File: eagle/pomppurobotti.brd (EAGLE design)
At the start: 66.3 x 70.5 mm, 23 parts, among them Q1 MOSFET-NCHANNELFQP30N06L

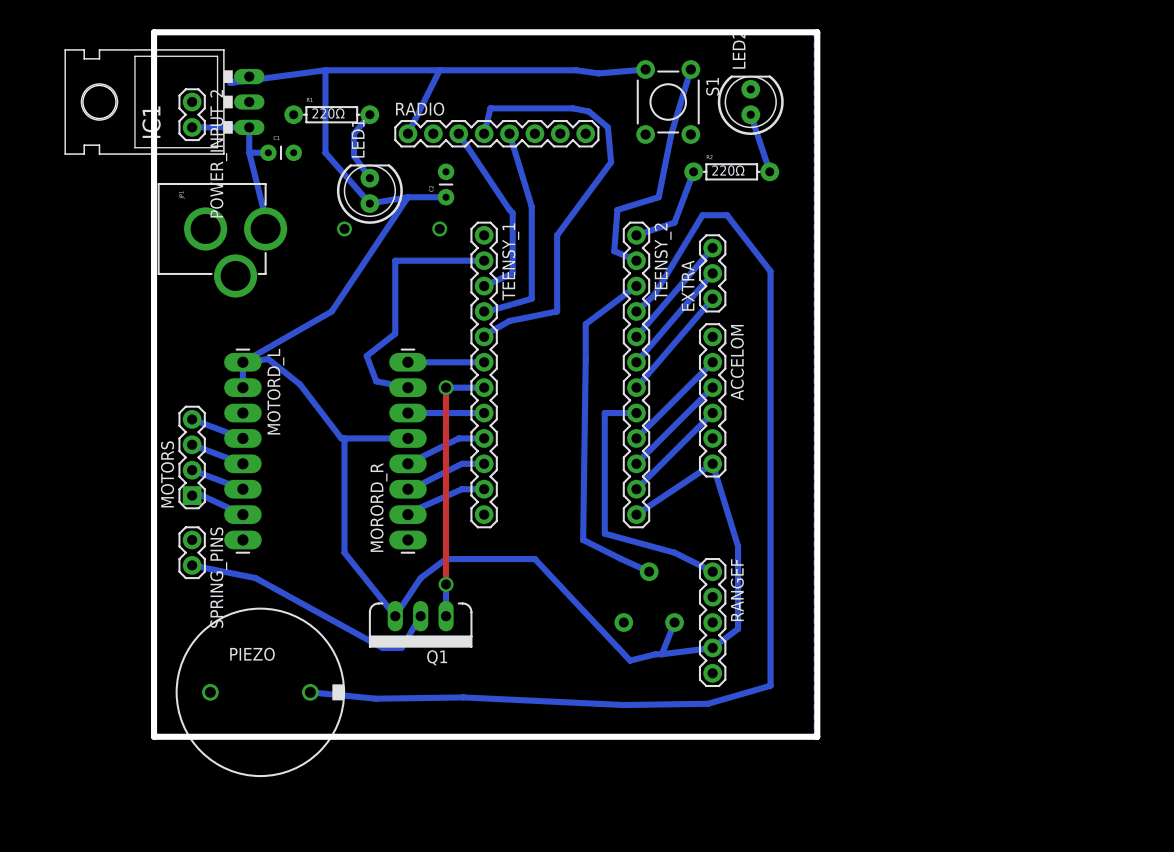
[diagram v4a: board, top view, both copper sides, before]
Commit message: Update the board to use voltage regulator only for Teensy and sensors
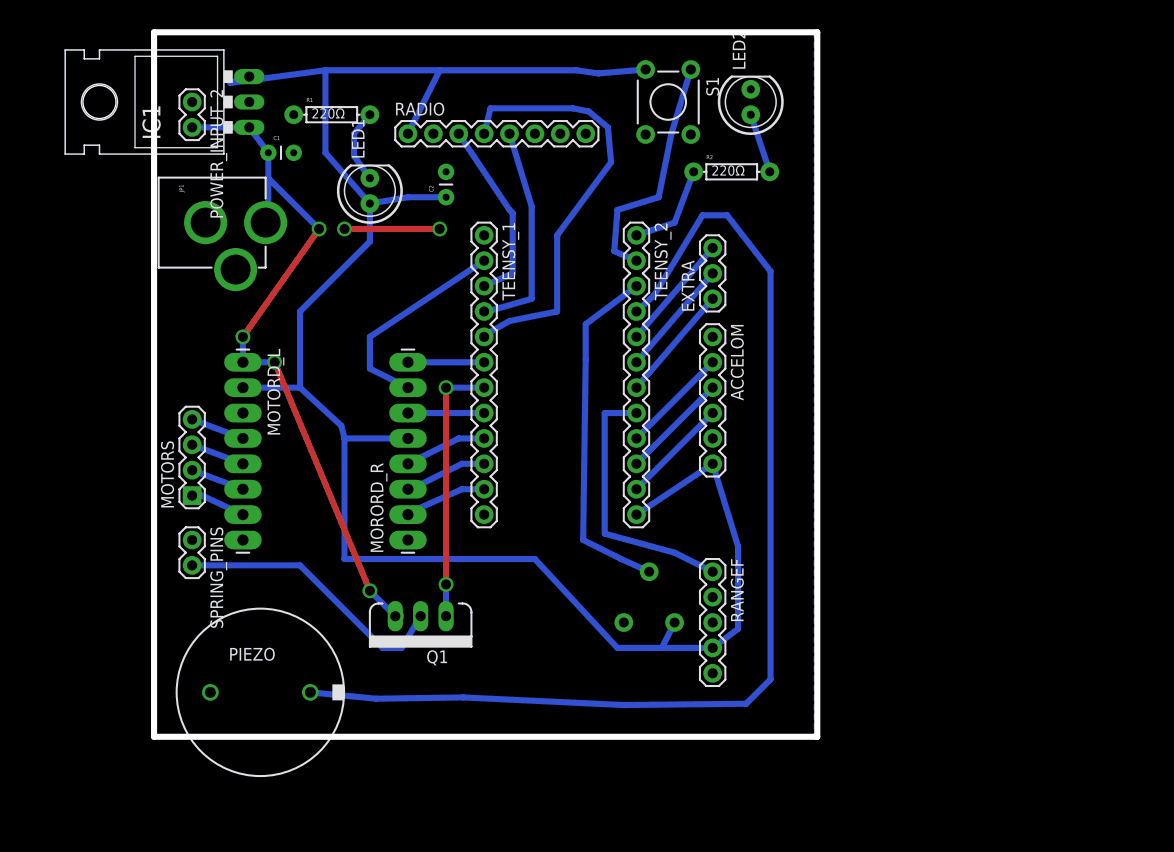
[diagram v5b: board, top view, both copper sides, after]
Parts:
- moved JP1 0.63 mm to (-2.54, 61.0)
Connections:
- removed net N$3: C1.1, IC1.IN, JP1.PWR, POWER_INPUT_2.2
- new net V_BATT: C1.1, IC1.IN, JP1.PWR, MOTORD_L.1, POWER_INPUT_2.2, Q1.3
- net VCC: no longer MOTORD_L.1, Q1.3
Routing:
- net V_BATT: track 0.00 -> 70.9 mm, vias 0 -> 4
- net N$3: track 18.0 -> 0.00 mm
- net VCC: track 211.2 -> 198.6 mm
- net GND: track 0.00 -> 9.52 mm
- net AIN2: track 25.8 -> 21.2 mm
- net N$5: track 26.6 -> 28.1 mm

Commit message: Add Arduino tests and modified RF library. Update Eagle schematics.
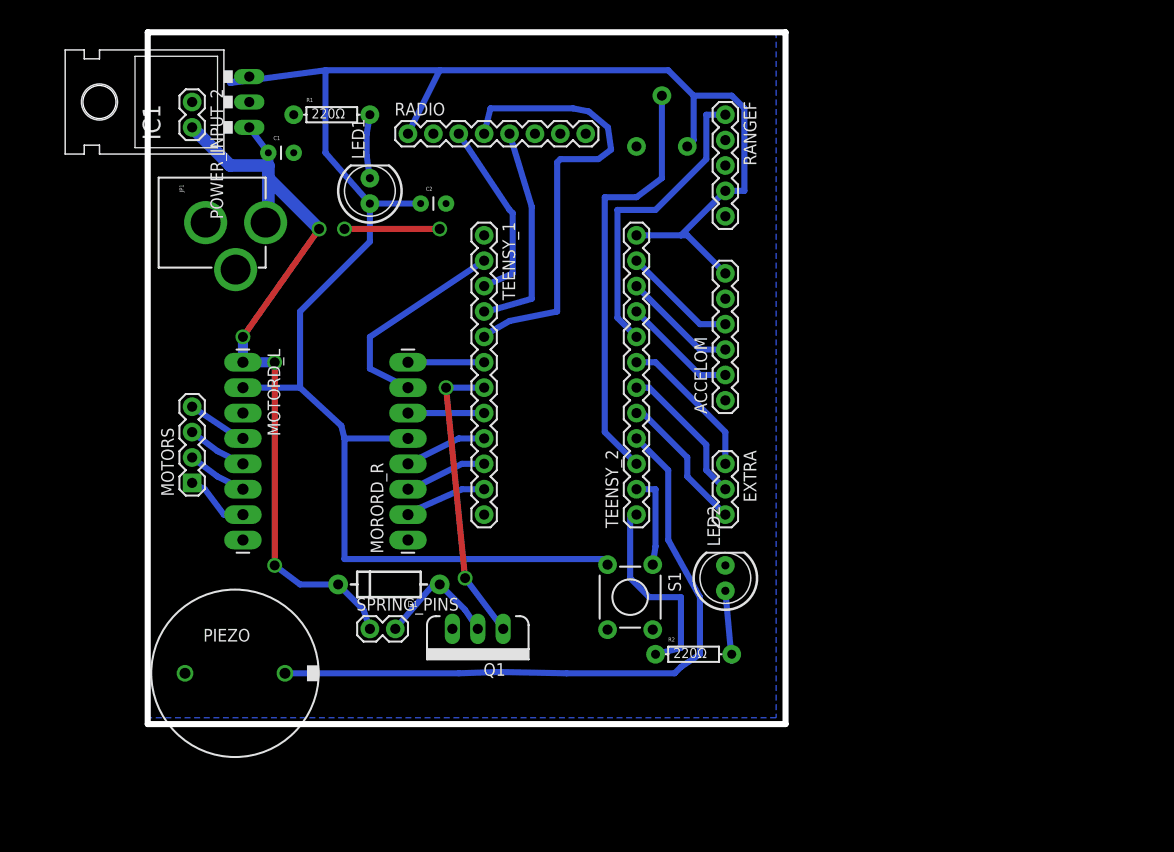
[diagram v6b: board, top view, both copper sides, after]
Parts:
- added D1: (no value), SparkFun-DiscreteSemi:DIODE-1N4001
- moved S1 49.7 mm to (47.6, 23.5)
- moved R2 48.4 mm to (54.0, 17.8)
- moved LED2 47.7 mm to (57.1, 25.4)
- moved RV1 47.6 mm to (50.8, 68.6)
- moved RANGEF 45.7 mm to (57.1, 71.8)
- moved TEENSY_2 27.9 mm to (48.3, 31.8), turned to 90 degrees
- moved SPRING_PINS 19.9 mm to (21.6, 20.3), turned to 0 degrees
- moved EXTRA 16.6 mm to (57.1, 36.8), turned to 270 degrees
- moved ACCELOM 6.48 mm to (57.1, 43.2), turned to 90 degrees
- moved Q1 5.85 mm to (32.4, 20.3)
- moved PIEZO 3.17 mm to (8.10, 15.9)
- moved C2 2.62 mm to (26.7, 62.9), turned to 0 degrees
- moved MOTORS 1.27 mm to (3.81, 34.9)
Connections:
- net GND: now also Q1.3; no longer SPRING_PINS.1
- net N$5: now also D1.A
- net V_BATT: now also D1.C, SPRING_PINS.1; no longer Q1.3
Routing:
- net PWMA7: track 109.2 -> 65.9 mm
- net N$5: track 28.1 -> 12.4 mm
- net PWMA9: track 24.1 -> 9.47 mm
- net LEDA10: track 9.44 -> 20.6 mm
- net V_BATT: track 70.9 -> 78.7 mm
- net A8: track 35.3 -> 42.6 mm
- net VCC: track 198.6 -> 193.6 mm
- net AN: track 26.7 -> 30.8 mm
- net A4: track 11.7 -> 15.6 mm
- net A5: track 11.7 -> 14.6 mm
- net MISO: track 43.0 -> 45.9 mm
- net PWMC: track 26.7 -> 29.3 mm
- net PWMA6: track 11.7 -> 14.2 mm
- net N$4: track 6.02 -> 7.65 mm
- net N$2: track 7.43 -> 6.40 mm
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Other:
- board size 66.3 x 70.5 mm -> 63.8 x 69.2 mm
